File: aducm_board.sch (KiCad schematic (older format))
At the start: 5 parts, among them U1 aducm_355

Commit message: Hopefully fixed issues with libraries not linking correctly
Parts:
- U1: footprint aducm_board:aducm355 -> ADUCM355:aducm355
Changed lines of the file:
@@
 F 0 "U1" H 5700 5515 50  0000 C CNN
 F 1 "aducm_355" H 5700 5424 50  0000 C CNN
-F 2 "aducm_board:aducm355" H 5700 3550 50  0001 C CNN
+F 2 "ADUCM355:aducm355" H 5700 3550 50  0001 C CNN
 F 3 "" H 5700 3550 50  0001 C CNN
 	1    5650 3600

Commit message: FTDI Added
Added ftdi and usb in
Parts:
- added C? (x4): 0.1uF, symbol Device:C
- added FB? (x2): Ferrite_Bead_Small, symbol Device:Ferrite_Bead_Small
- added J?: USB_B_Micro, symbol Connector:USB_B_Micro
- added JP? (x2): Jumper_NC_Small, symbol Device:Jumper_NC_Small
- added U?: FT232RL, Package_SO:SSOP-28_5.3x10.2mm_P0.65mm, symbol Interface_USB:FT232RL
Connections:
- net labels added: 3V3VOUT, 5VUSB, AGND, DGND, GNDA, GNDD, P0.10_SOUT, P0.11_SIN, USBD+, USBD-
- wire segments 30 -> 78
- no-connect marks 4 -> 16
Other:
- moved on the sheet: U1

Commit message: Started making connections to the 355
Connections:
- net labels added: DVDD, P1.5_CS, SWDIO
- net labels removed: GND
- wire segments 78 -> 88
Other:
- note added: "FTDI USB to UART"
- note added: "Nets"
- note added: "USB Input"
- moved on the sheet: C?, FB?, J?, JP?, R?, U?

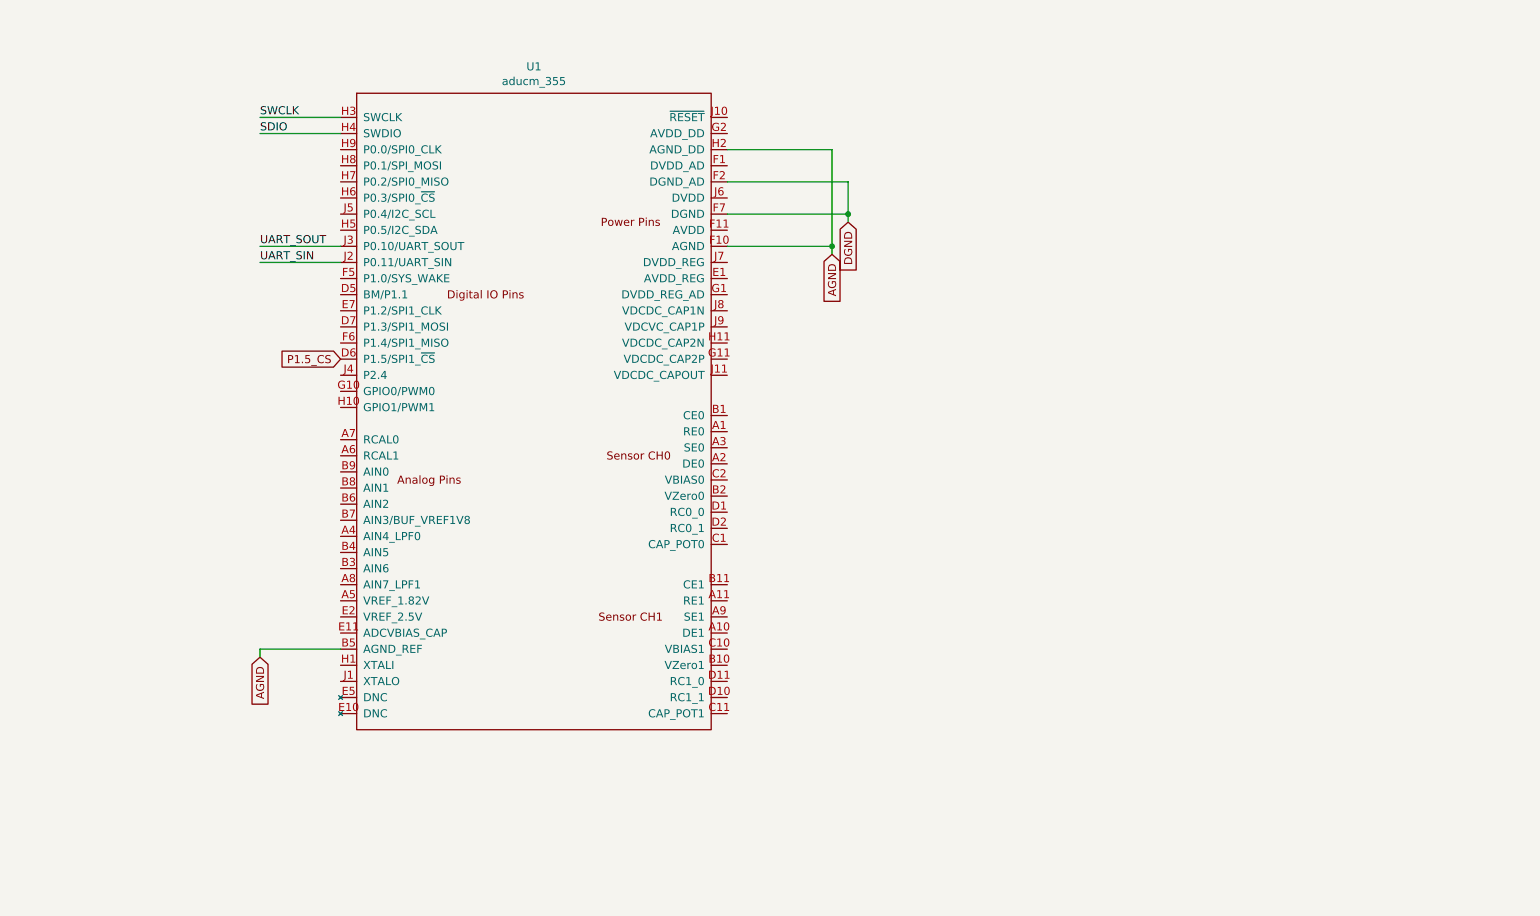
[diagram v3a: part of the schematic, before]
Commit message: Added subsheet for EC Sensors
Also continued to populate the board with components
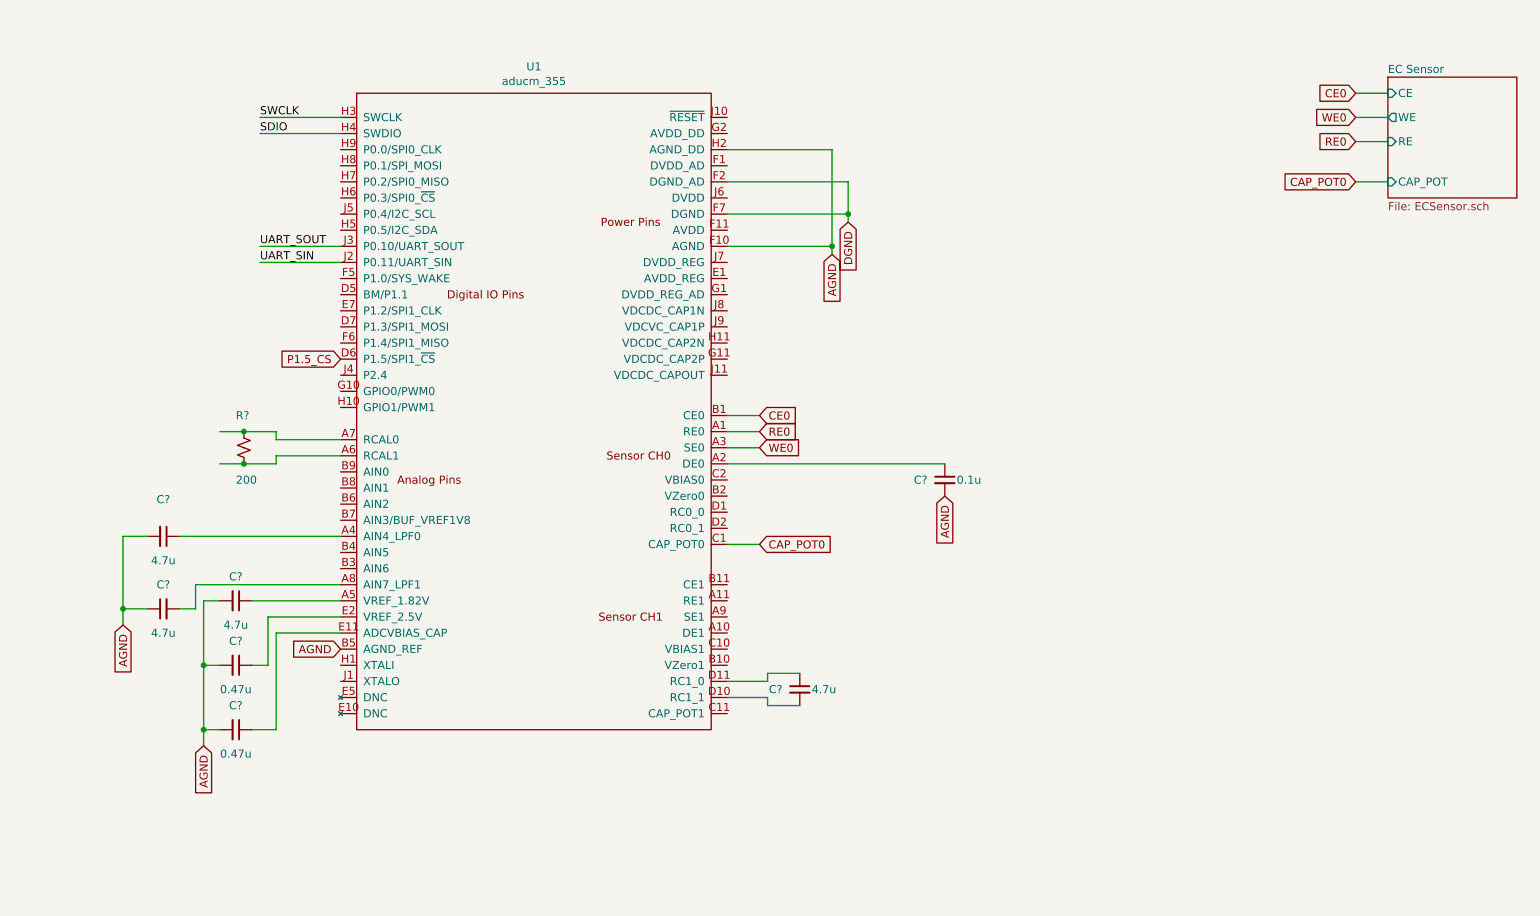
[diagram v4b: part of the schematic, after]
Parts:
- added C? (x4): 4.7u, symbol Device:C_Small
- added C? (x2): 0.47u, symbol Device:C_Small
- added C?: 0.1u, symbol Device:C_Small
- added R?: 200, symbol Device:R_Small_US
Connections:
- net GNDA: now also C?.1, C?.2, C?.2, C?.2, C?.2, C?.2
- net RE0: now reaches U1.A1 (RE0)
- net at U1.A2 (DE0): now also C?.1
- net WE0: now reaches U1.A3 (SE0)
- net at U1.A4 (AIN4_LPF0): now also C?.1
- net at U1.A5 (VREF_1.82V): now also C?.1
- net at U1.A6 (RCAL1): now also R?.2
- net at U1.A7 (RCAL0): now also R?.1
- net at U1.A8 (AIN7_LPF1): now also C?.2
- net CE0: now reaches U1.B1 (CE0)
- net CAP_POT0: now reaches U1.C1 (CAP_POT0)
- net at U1.D10 (RC1_1): now also C?.2
- net at U1.D11 (RC1_0): now also C?.1
- net at U1.E11 (ADCVBIAS_CAP): now also C?.1
- net at U1.E2 (VREF_2.5V): now also C?.1
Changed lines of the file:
@@
 $Descr A3 16535 11693
 encoding utf-8
-Sheet 1 1
+Sheet 1 2
 Title ""
 Date ""
@@
 Wire Wire Line
 	11400 1950 11400 2000
-Wire Wire Line
-	8350 4450 7850 4450
-Wire Wire Line
-	7850 4450 7850 4500
-Text GLabel 7850 4500 3    50   Input ~ 0
+Text GLabel 8350 4450 0    50   Input ~ 0
 AGND
 Text GLabel 1300 10700 3    50   Input ~ 0
@@
 Wire Wire Line
 	1300 1550 1550 1550
+Text GLabel 7000 4300 3    50   Input ~ 0
+AGND
+$Comp
+L Device:C_Small C?
+U 1 1 5DE9C21A
+P 7250 3750
+F 0 "C?" V 7021 3750 50  0000 C CNN
+F 1 "4.7u" V 7400 3750 50  0000 C CNN
+F 2 "" H 7250 3750 50  0001 C CNN
+F 3 "~" H 7250 3750 50  0001 C CNN
+	1    7250 3750
+	0    1    1    0
+$EndComp
+$Comp
+L Device:C_Small C?
+U 1 1 5DEBDEC6
+P 7700 4950
+F 0 "C?" V 7550 4950 50  0000 C CNN
+F 1 "0.47u" V 7850 4950 50  0000 C CNN
+F 2 "" H 7700 4950 50  0001 C CNN
+F 3 "~" H 7700 4950 50  0001 C CNN
+	1    7700 4950
+	0    1    1    0
+$EndComp
+$Comp
+L Device:C_Small C?
+U 1 1 5DEBEC2A
+P 7700 4550
+F 0 "C?" V 7550 4550 50  0000 C CNN
+F 1 "0.47u" V 7850 4550 50  0000 C CNN
+F 2 "" H 7700 4550 50  0001 C CNN
+F 3 "~" H 7700 4550 50  0001 C CNN
+	1    7700 4550
+	0    1    1    0
+$EndComp
+$Comp
+L Device:C_Small C?
+U 1 1 5DEBE767
+P 7700 4150
+F 0 "C?" V 7550 4150 50  0000 C CNN
+F 1 "4.7u" V 7850 4150 50  0000 C CNN
+F 2 "" H 7700 4150 50  0001 C CNN
+F 3 "~" H 7700 4150 50  0001 C CNN
+	1    7700 4150
+	0    1    1    0
+$EndComp
+Wire Wire Line
+	8350 4350 7950 4350
+Wire Wire Line
+	7800 4150 8350 4150
+Wire Wire Line
+	8350 4250 7900 4250
+Wire Wire Line
+	7900 4250 7900 4550
+Wire Wire Line
+	7900 4550 7800 4550
+Wire Wire Line
+	7950 4350 7950 4950
+Wire Wire Line
+	7950 4950 7800 4950
+Text GLabel 7500 5050 3    50   Input ~ 0
+AGND
+Wire Wire Line
+	7600 4950 7500 4950
+Wire Wire Line
+	7500 4950 7500 5050
+Wire Wire Line
+	7600 4550 7500 4550
+Wire Wire Line
+	7500 4550 7500 4950
+Connection ~ 7500 4950
+Wire Wire Line
+	7600 4150 7500 4150
+Wire Wire Line
+	7500 4150 7500 4550
+Connection ~ 7500 4550
+$Comp
+L Device:C_Small C?
+U 1 1 5DF008D1
+P 11200 4700
+F 0 "C?" H 11050 4700 50  0000 C CNN
+F 1 "4.7u" H 11350 4700 50  0000 C CNN
+F 2 "" H 11200 4700 50  0001 C CNN
+F 3 "~" H 11200 4700 50  0001 C CNN
+	1    11200 4700
+	1    0    0    -1
+$EndComp
+Wire Wire Line
+	10750 4650 11000 4650
+Wire Wire Line
+	11000 4650 11000 4600
+Wire Wire Line
+	11000 4600 11200 4600
+Wire Wire Line
+	10750 4750 11000 4750
+Wire Wire Line
+	11000 4750 11000 4800
+Wire Wire Line
+	11000 4800 11200 4800
+$Comp
+L Device:C_Small C?
+U 1 1 5DF0CBC7
+P 7250 4200
+F 0 "C?" V 7400 4200 50  0000 C CNN
+F 1 "4.7u" V 7100 4200 50  0000 C CNN
+F 2 "" H 7250 4200 50  0001 C CNN
+F 3 "~" H 7250 4200 50  0001 C CNN
+	1    7250 4200
+	0    -1   -1   0
+$EndComp
+Wire Wire Line
+	7000 3750 7150 3750
+Wire Wire Line
+	7350 3750 8350 3750
+Wire Wire Line
+	7150 4200 7000 4200
+Wire Wire Line
+	7000 4200 7000 4300
+Connection ~ 7000 4200
+Wire Wire Line
+	7000 3750 7000 4200
+Wire Wire Line
+	7450 4200 7350 4200
+Wire Wire Line
+	7450 4200 7450 4050
+Wire Wire Line
+	7450 4050 8350 4050
+$Comp
+L Device:R_Small_US R?
+U 1 1 5DF5272B
+P 7750 3200
+F 0 "R?" H 7700 3400 50  0000 L CNN
+F 1 "200" H 7700 3000 50  0000 L CNN
+F 2 "" H 7750 3200 50  0001 C CNN
+F 3 "~" H 7750 3200 50  0001 C CNN
+	1    7750 3200
+	1    0    0    -1
+$EndComp
+Wire Wire Line
+	8350 3150 7950 3150
+Wire Wire Line
+	7950 3150 7950 3100
+Wire Wire Line
+	7950 3100 7750 3100
+Wire Wire Line
+	8350 3250 7950 3250
+Wire Wire Line
+	7950 3250 7950 3300
+Wire Wire Line
+	7950 3300 7750 3300
+Wire Wire Line
+	7600 3100 7750 3100
+Connection ~ 7750 3100
+Wire Wire Line
+	7750 3300 7600 3300
+Connection ~ 7750 3300
+$Sheet
+S 14850 900  800  750
+U 5DF7340A
+F0 "EC Sensor" 50
+F1 "ECSensor.sch" 50
+F2 "WE" O L 14850 1150 50
+F3 "RE" I L 14850 1300 50
+F4 "CAP_POT" I L 14850 1550 50
+F5 "CE" I L 14850 1000 50
+$EndSheet
+Text GLabel 14650 1000 0    50   Input ~ 0
+CE0
+Text GLabel 14650 1150 0    50   Input ~ 0
+WE0
+Text GLabel 14650 1300 0    50   Input ~ 0
+RE0
+Text GLabel 14650 1550 0    50   Input ~ 0
+CAP_POT0
+Wire Wire Line
+	14650 1000 14850 1000
+Wire Wire Line
+	14850 1150 14650 1150
+Wire Wire Line
+	14850 1300 14650 1300
+Wire Wire Line
+	14850 1550 14650 1550
+Text GLabel 10950 3800 2    50   Input ~ 0
+CAP_POT0
+Wire Wire Line
+	10950 3800 10750 3800
+Text GLabel 10950 3000 2    50   Input ~ 0
+CE0
+Text GLabel 10950 3100 2    50   Input ~ 0
+RE0
+Text GLabel 10950 3200 2    50   Input ~ 0
+WE0
+Wire Wire Line
+	10950 3000 10750 3000
+Wire Wire Line
+	10950 3100 10750 3100
+Wire Wire Line
+	10950 3200 10750 3200
+$Comp
+L Device:C_Small C?
+U 1 1 5DFD0379
+P 12100 3400
+F 0 "C?" H 11950 3400 50  0000 C CNN
+F 1 "0.1u" H 12250 3400 50  0000 C CNN
+F 2 "" H 12100 3400 50  0001 C CNN
+F 3 "~" H 12100 3400 50  0001 C CNN
+	1    12100 3400
+	1    0    0    -1
+$EndComp
+Wire Wire Line
+	12100 3300 10750 3300
+Text GLabel 12100 3500 3    50   Input ~ 0
+AGND
 $EndSCHEMATC

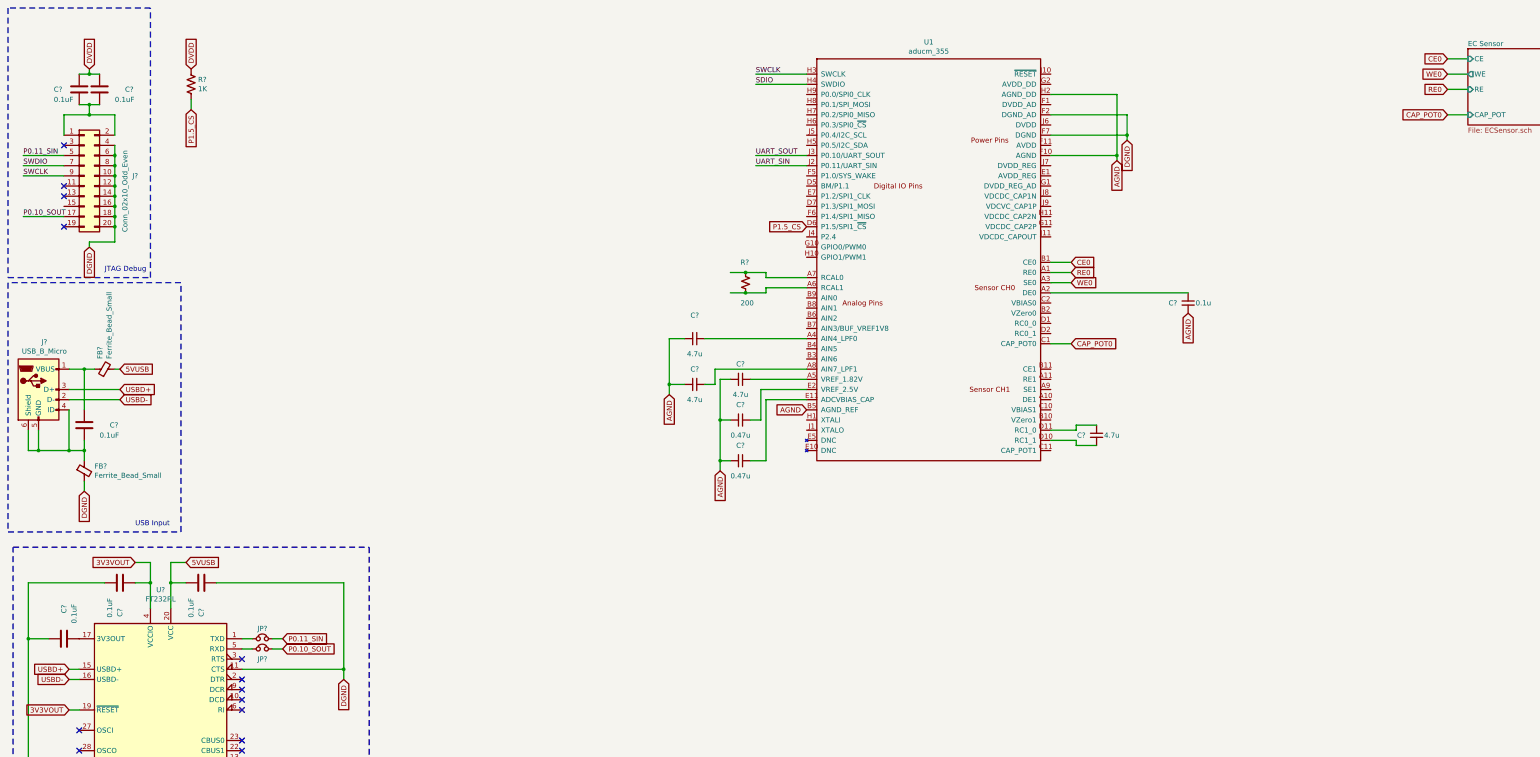
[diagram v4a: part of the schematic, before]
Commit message: More labels and connections added
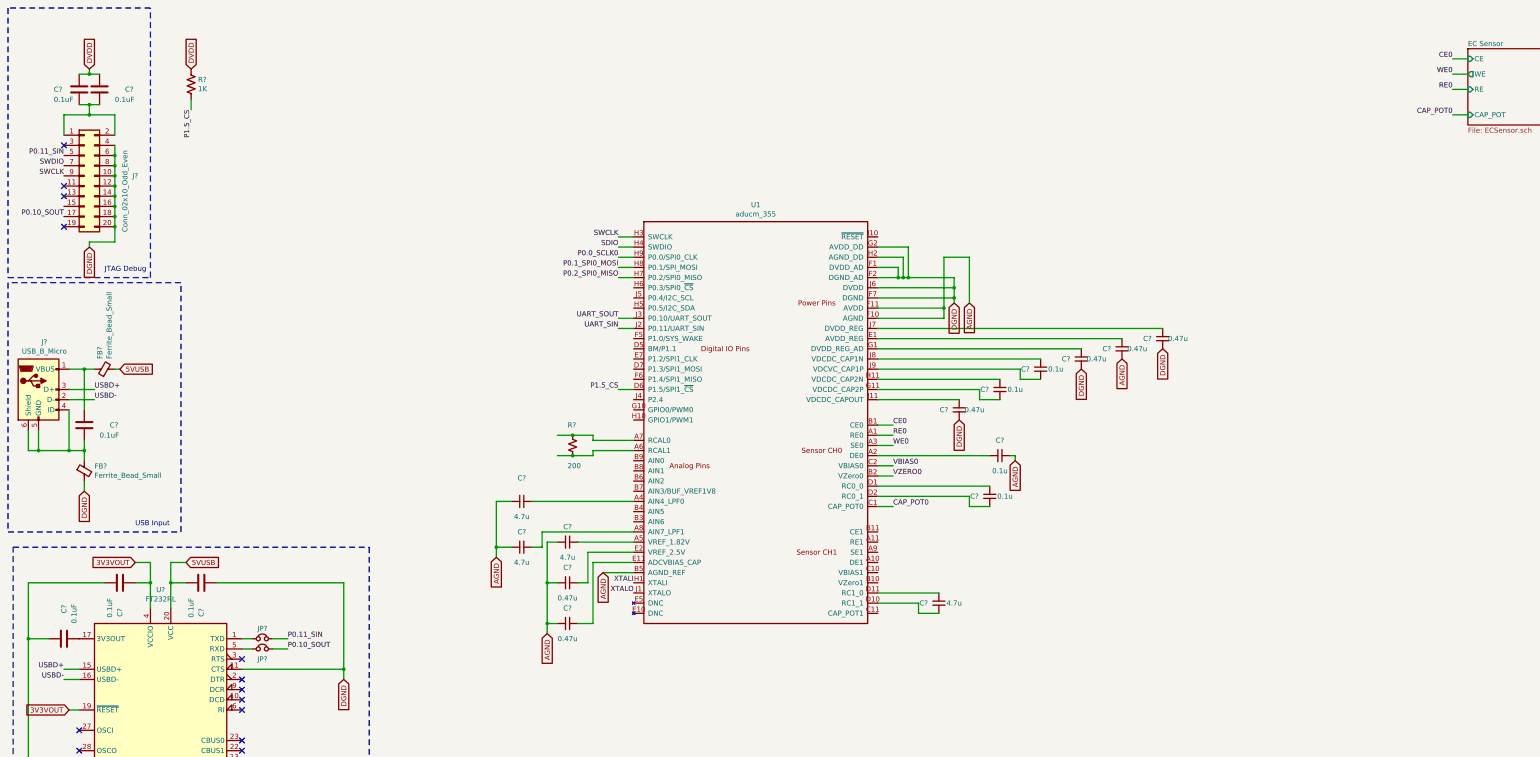
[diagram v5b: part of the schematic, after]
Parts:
- added C? (x4): 0.47u, symbol Device:C_Small
- added C? (x3): 0.1u, symbol Device:C_Small
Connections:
- net GNDA: now also C?.1, U1.F11 (AVDD), C?.2; no longer C?.2, U1.H2 (AGND_DD)
- net GNDD: now also U1.F1 (DVDD_AD), U1.G2 (AVDD_DD), U1.H2 (AGND_DD), U1.J6 (DVDD), C?.2, C?.2, C?.2
- net at U1.A2 (DE0): now also C?.2; no longer C?.1
- net VZERO0: now reaches U1.B2 (VZero0)
- net VBIAS0: now reaches U1.C2 (VBIAS0)
- net at U1.D1 (RC0_0): now also C?.1
- net at U1.D2 (RC0_1): now also C?.2
- net at U1.E1 (AVDD_REG): now also C?.1
- net at U1.G1 (DVDD_REG_AD): now also C?.1
- net at U1.G11 (VDCDC_CAP2P): now also C?.2
- net XTALI: now reaches U1.H1 (XTALI)
- net at U1.H11 (VDCDC_CAP2N): now also C?.1
- net P0.2_SPI0_MISO: now reaches U1.H7 (P0.2/SPI0_MISO)
- net P0.1_SPI0_MOSI: now reaches U1.H8 (P0.1/SPI_MOSI)
- net P0.0_SCLK0: now reaches U1.H9 (P0.0/SPI0_CLK)
- net XTALO: now reaches U1.J1 (XTALO)
- net at U1.J11 (VDCDC_CAPOUT~): now also C?.1
- net at U1.J7 (DVDD_REG): now also C?.1
- net at U1.J8 (VDCDC_CAP1N): now also C?.1
- net at U1.J9 (VDCVC_CAP1P): now also C?.2
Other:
- moved on the sheet: C?, R?, U1

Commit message: Mostly complete Schematic
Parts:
- removed C? (x2): 0.1uF, symbol Device:C
- removed J?: Conn_02x10_Odd_Even, symbol Connector_Generic:Conn_02x10_Odd_Even
- removed R?: 1K, symbol Device:R_US
- added BT?: 3.3V, symbol Device:Battery
- added C? (x7): 0.1uF, symbol Device:C
- added C?: 220pF, symbol Device:C
- added C? (x2): 0.1u, symbol Device:C_Small
- added C? (x2): 7pF, symbol Device:C
- added C?: 10u, symbol Device:C_Small
- added J?: Conn_02x04_Odd_Even, symbol Connector_Generic:Conn_02x04_Odd_Even
- added R? (x3): 0, symbol Device:R_Small_US
- added R? (x2): 100k, symbol Device:R_Small_US
- added SW?: SW_Push, symbol Switch:SW_Push
- added SW?: SW_SPST, symbol Switch:SW_SPST
- added Y?: Crystal_GND24, symbol Device:Crystal_GND24
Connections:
- net 3V3VOUT: now also C?.2, U?.17 (3V3OUT)
- net CAP_POT0: now also U1.C11 (CAP_POT1)
- net GNDA: now also C?.1, C?.1, C?.2, C?.2, C?.2, C?.2, FB?.2, U1.F2 (DGND_AD), U1.F7 (DGND), U1.H2 (AGND_DD), U?.11 (CTS), U?.18 (GND), U?.21 (GND), U?.25 (AGND), U?.26 (TEST), U?.7 (GND), BT?.2 (-), C?.1, C?.2, C?.2, C?.2, C?.2, C?.2, C?.2, C?.2, C?.2, C?.2, C?.2, J?.2 (Pin_2), SW?.2, Y?.2, Y?.4; no longer U1.F11 (AVDD)
- net P0.10_SOUT: now also J?.4 (Pin_4)
- net P0.11_SIN: now also J?.6 (Pin_6)
- net SWCLK: now also J?.5 (Pin_5), R?.2
- net SWDIO: now also J?.3 (Pin_3), R?.2
- net VBIAS0: now also C?.1
- net VZERO0: now also C?.1
- net XTALI: now also C?.1, Y?.1
- net XTALO: now also C?.1, Y?.3
- net at U1.A10 (DE1): now also C?.2
- net at U1.A11 (RE1): now also R?.2
- net at U1.A9 (SE1): now also R?.2
- net at U1.B11 (CE1): now also R?.2
- net ~RESET: now reaches U1.J10 (~RESET~)
- net ~RESET: now also J?.1 (Pin_1), SW?.1
- removed net GNDD: C?.1, C?.1, C?.2, C?.2, C?.2, C?.2, FB?.2, U1.F1 (DVDD_AD), U1.F2 (DGND_AD), U1.F7 (DGND), U1.G2 (AVDD_DD), U1.H2 (AGND_DD), U1.J6 (DVDD), U?.11 (CTS), U?.18 (GND), U?.21 (GND), U?.25 (AGND), U?.26 (TEST), U?.7 (GND)
- new net AIN3: C?.1
- new net AVDD: C?.1, U1.F11 (AVDD)
- new net CE1: R?.1
- new net DVDD: C?.1, C?.1, J?.8 (Pin_8), R?.1, R?.1, U1.F1 (DVDD_AD), U1.G2 (AVDD_DD), U1.J6 (DVDD)
- new net RE1: R?.1
- new net VBAT: BT?.1 (+), SW?.1 (A)
- new net VBIAS1: C?.1
- new net VZERO1: C?.1
- new net WE1: R?.1
- no-connect marks 16 -> 12
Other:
- note added: "6-pin J-Tag Connector"
- note added: "Decoupling Caps where space was tight"
- note added: "External Crystal\n"
- note added: "MCU Reset"
- note removed: "JTAG Debug"
- moved on the sheet: C?, FB?, J?, JP?, R?, U1, U?
